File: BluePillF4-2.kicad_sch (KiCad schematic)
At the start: 15 parts, among them J6 Conn_Coaxial, Q1 IRLML6402, U1 AP2114HA-3.3TRG1, U2 AP2112K3.3-TRG1, U5 MCP73812T-420I/OT, U6 RFM95W-868S2

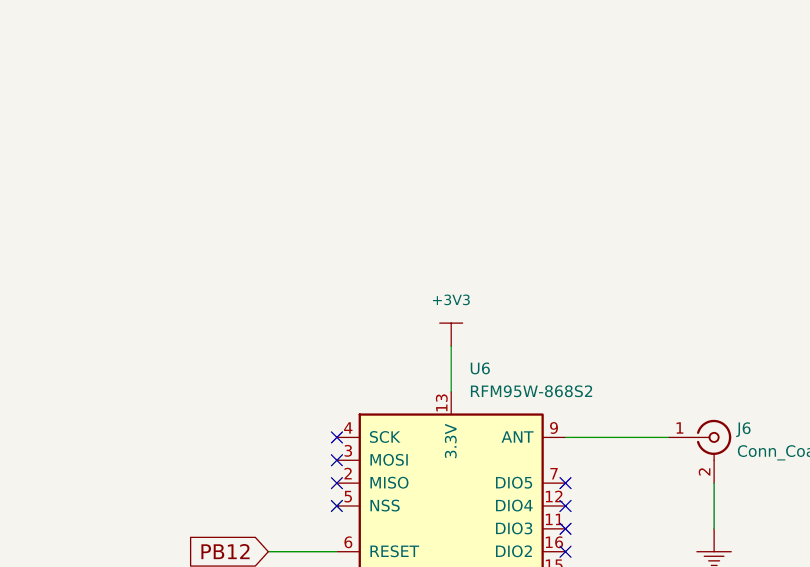
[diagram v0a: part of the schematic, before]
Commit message: adding 3D shape for Molex 73251-1153 SMA Connector
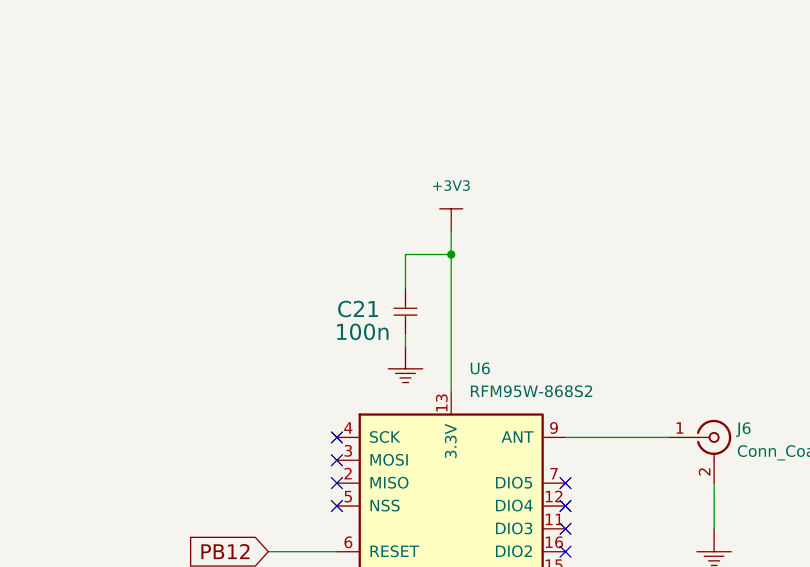
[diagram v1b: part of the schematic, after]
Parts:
- added C21: 100n, BluePillF4 Lib:C0603, symbol BluePillF4:CAP_0603
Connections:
- net +3V3: now also C21.2
- net GND: now also C21.1
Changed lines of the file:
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@@
   (junction (at 184.15 29.21) (diameter 0) (color 0 0 0 0)
+  )
+  (junction (at 76.2 116.84) (diameter 0) (color 0 0 0 0)
   )
   (junction (at 66.04 71.12) (diameter 0) (color 0 0 0 0)
@@
     (stroke (width 0) (type default) (color 0 0 0 0))
   )
-  (wire (pts (xy 76.2 127) (xy 76.2 132.08))
+  (wire (pts (xy 76.2 114.3) (xy 76.2 116.84))
     (stroke (width 0) (type default) (color 0 0 0 0))
   )
@@
     (stroke (width 0) (type default) (color 0 0 0 0))
   )
+  (wire (pts (xy 71.12 116.84) (xy 76.2 116.84))
+    (stroke (width 0) (type default) (color 0 0 0 0))
+  )
   (wire (pts (xy 27.94 55.88) (xy 30.48 55.88))
     (stroke (width 0) (type default) (color 0 0 0 0))
   )
+  (wire (pts (xy 76.2 116.84) (xy 76.2 132.08))
+    (stroke (width 0) (type default) (color 0 0 0 0))
+  )
   (wire (pts (xy 66.04 71.12) (xy 76.2 71.12))
     (stroke (width 0) (type default) (color 0 0 0 0))
@@
     (stroke (width 0) (type default) (color 0 0 0 0))
   )
+  (wire (pts (xy 71.12 120.65) (xy 71.12 116.84))
+    (stroke (width 0) (type default) (color 0 0 0 0))
+  )
   (wire (pts (xy 76.2 160.02) (xy 76.2 163.83))
     (stroke (width 0) (type default) (color 0 0 0 0))
@@
   )
   (wire (pts (xy 43.18 71.12) (xy 58.42 71.12))
+    (stroke (width 0) (type default) (color 0 0 0 0))
+  )
+  (wire (pts (xy 71.12 125.73) (xy 71.12 127))
     (stroke (width 0) (type default) (color 0 0 0 0))
   )
@@
     (pin "~")
   )
+  (symbol (lib_id "BluePillF4:GND") (at 71.12 127 0) (unit 1)
+    (in_bom yes) (on_board yes) (fields_autoplaced)
+    (property "Reference" "#SUPPLY0102" (id 0) (at 71.12 127 0)
+      (effects (font (size 1.143 1.143)) (justify left bottom) hide)
+    )
+    (property "Value" "" (id 1) (at 71.12 133.35 0)
+      (effects (font (size 1.143 1.143)))
+    )
+    (property "Footprint" "" (id 2) (at 71.12 127 0)
+      (effects (font (size 1.524 1.524)) hide)
+    )
+    (property "Datasheet" "" (id 3) (at 71.12 127 0)
+      (effects (font (size 1.524 1.524)) hide)
+    )
+    (pin "~")
+  )
   (symbol (lib_id "BluePillF4:GND") (at 76.2 168.91 0) (unit 1)
     (in_bom yes) (on_board yes) (fields_autoplaced)
@@
     (pin "~")
   )
-  (symbol (lib_id "BluePillF4:+3V3") (at 76.2 127 0) (unit 1)
+  (symbol (lib_id "BluePillF4:+3V3") (at 76.2 114.3 0) (unit 1)
     (in_bom yes) (on_board yes) (fields_autoplaced)
-    (property "Reference" "#SUPPLY019" (id 0) (at 76.2 127 0)
+    (property "Reference" "#SUPPLY019" (id 0) (at 76.2 114.3 0)
       (effects (font (size 1.143 1.143)) (justify left bottom) hide)
     )
-    (property "Value" "+3V3" (id 1) (at 76.2 121.92 0)
+    (property "Value" "+3V3" (id 1) (at 76.2 109.22 0)
       (effects (font (size 1.143 1.143)))
     )
-    (property "Footprint" "" (id 2) (at 76.2 127 0)
-      (effects (font (size 1.524 1.524)) hide)
-    )
-    (property "Datasheet" "" (id 3) (at 76.2 127 0)
+    (property "Footprint" "" (id 2) (at 76.2 114.3 0)
+      (effects (font (size 1.524 1.524)) hide)
+    )
+    (property "Datasheet" "" (id 3) (at 76.2 114.3 0)
       (effects (font (size 1.524 1.524)) hide)
     )
@@
     (pin "9")
   )
+  (symbol (lib_id "BluePillF4:CAP_0603") (at 71.12 123.19 270) (mirror x) (unit 1)
+    (in_bom yes) (on_board yes)
+    (property "Reference" "C21" (id 0) (at 63.5 121.92 90)
+      (effects (font (size 1.778 1.778)) (justify left bottom))
+    )
+    (property "Value" "100n" (id 1) (at 63.246 124.46 90)
+      (effects (font (size 1.778 1.778)) (justify left bottom))
+    )
+    (property "Footprint" "BluePillF4 Lib:C0603" (id 2) (at 65.786 123.444 0)
+      (effects (font (size 1.651 1.651)) (justify left top) hide)
+    )
+    (property "Datasheet" "" (id 3) (at 71.12 123.19 0)
+      (effects (font (size 1.524 1.524)) hide)
+    )
+    (property "TOL" "±10%" (id 4) (at 71.12 123.19 0)
+      (effects (font (size 1.524 1.524)) hide)
+    )
+    (property "VOLT" "50V" (id 5) (at 71.12 123.19 0)
+      (effects (font (size 1.524 1.524)) hide)
+    )
+    (property "PARTNO" "C0603_100n_X7R_10%_CER_50V" (id 6) (at 71.12 123.19 0)
+      (effects (font (size 1.524 1.524)) hide)
+    )
+    (property "TYPE" "CER" (id 7) (at 71.12 123.19 0)
+      (effects (font (size 1.524 1.524)) hide)
+    )
+    (property "TC" "X7R" (id 8) (at 71.12 123.19 0)
+      (effects (font (size 1.524 1.524)) hide)
+    )
+    (property "SIZE" "0603" (id 9) (at 71.12 123.19 0)
+      (effects (font (size 1.524 1.524)) hide)
+    )
+    (property "DNP" "F" (id 10) (at 71.12 123.19 0)
+      (effects (font (size 1.524 1.524)) hide)
+    )
+    (property "AliExpress" "https://www.aliexpress.com/item/0603-SMD-Capacitor-assorted-kit-36values-20pcs-720pcs-1pF-10uF-Samples-Kit-electronic-diy-kit/32817046315.html" (id 11) (at 71.12 123.19 0)
+      (effects (font (size 1.524 1.524)) hide)
+    )
+    (pin "1")
+    (pin "2")
+  )
 )

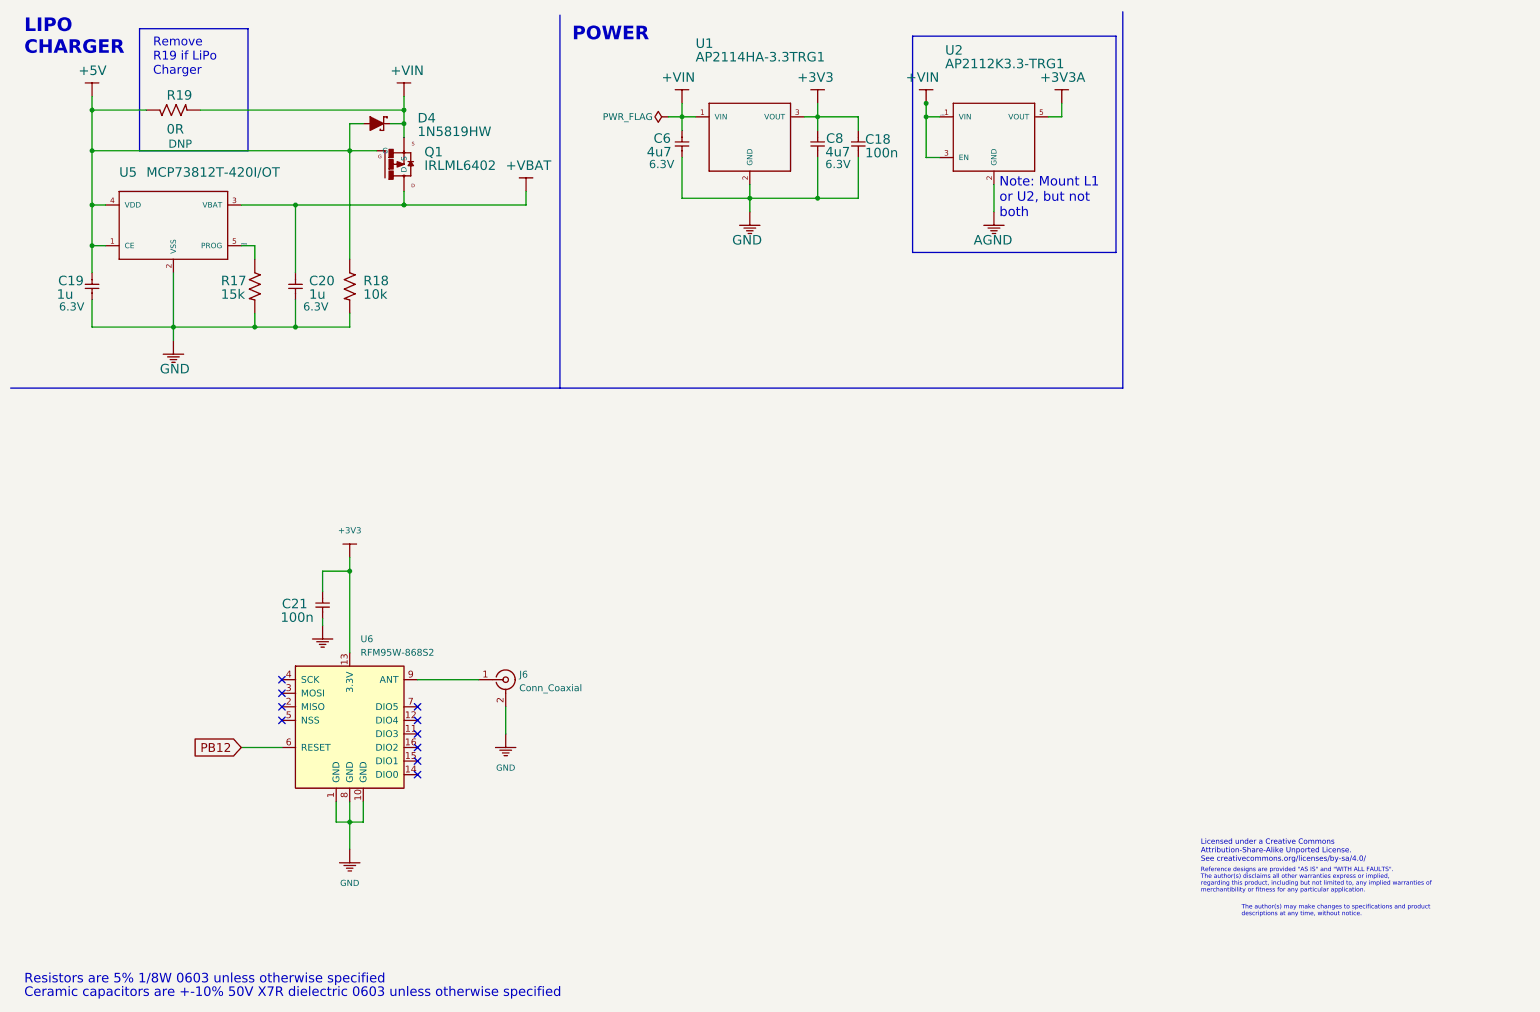
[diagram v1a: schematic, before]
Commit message: Removed unnecessary components like LiPo charger and fixed most errors. First connections between LoRa module and MCU created in the schematic.
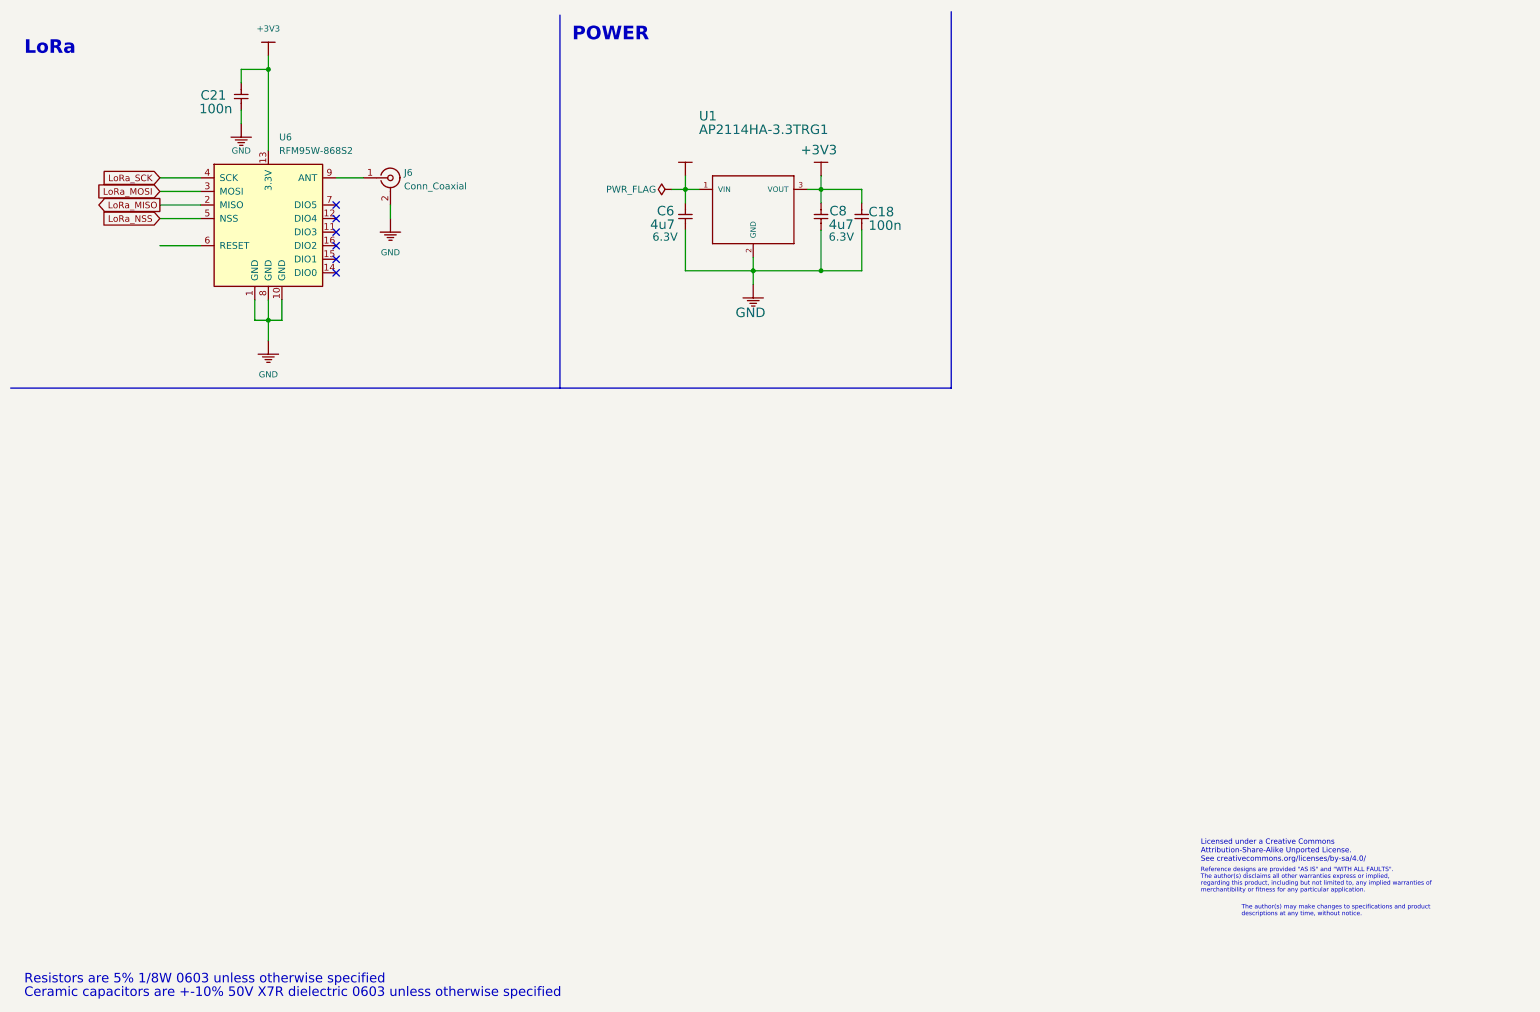
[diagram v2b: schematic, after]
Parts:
- removed C19, C20: 1u, BluePillF4 Lib:C0603, symbol BluePillF4:CAP_0603
- removed D4: 1N5819HW, BluePillF4 Lib:SOD-123, symbol BluePillF4:1N5819HW
- removed Q1: IRLML6402, BluePillF4 Lib:SOT323, symbol BluePillF4:IRLML6402
- removed R17: 15k, BluePillF4 Lib:R0603, symbol BluePillF4:RES_0603
- removed R18: 10k, BluePillF4 Lib:R0603, symbol BluePillF4:RES_0603
- removed R19: 0R, BluePillF4 Lib:R0603, symbol BluePillF4:RES_0603
- removed U2: AP2112K3.3-TRG1, BluePillF4 Lib:SOT23-5, symbol BluePillF4:AP2112K3.3-TRG1
- removed U5: MCP73812T-420I/OT, BluePillF4 Lib:SOT23-5, symbol BluePillF4:MCP73812T-420I/OT
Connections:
- net +VIN is gone; now on net +5V: C6.1, U1.1 (VIN)
- net LoRa_MISO: now reaches U6.2 (MISO)
- net LoRa_MOSI: now reaches U6.3 (MOSI)
- net LoRa_SCK: now reaches U6.4 (SCK)
- net LoRa_NSS: now reaches U6.5 (NSS)
- net PB12: no longer names the net of U6.6 (RESET)
- no-connect marks 10 -> 6
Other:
- note added: "LoRa"
- note removed: "LIPO CHARGER"
- note removed: "Note: Mount L1 or U2, but not both"
- note removed: "Remove R19 if LiPo Charger"
- moved on the sheet: C18, C21, C6, C8, J6, U1, U6

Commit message: Delete the RTC oscillator. First routing of the LoRa module.
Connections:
- no-connect marks 6 -> 7
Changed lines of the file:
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@@
   (no_connect (at 73.66 58.42))
   (no_connect (at 73.66 48.26))
+  (no_connect (at 40.64 55.88))
   (wire (pts (xy 161.925 45.339) (xy 164.465 45.339))
     (stroke (width 0) (type default) (color 0 0 0 0))
@@
       (effects (font (size 1.143 1.143)) (justify left bottom) hide)
     )
-    (property "Value" "" (id 1) (at 139.065 38.1 0)
+    (property "Value" "+5V" (id 1) (at 139.065 38.1 0)
       (effects (font (size 1.143 1.143)))
     )
